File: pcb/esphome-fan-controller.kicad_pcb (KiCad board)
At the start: 2 copper layers, 25 x 42.5 mm, 50 parts, among them J1 Screw_Terminal_01x02, J2 USB-C, M1 Fan_CPU_4pin, SW1 BOOT, SW2 RESET, U1 MPM3506AGQV-P, U2 TPS61322DBZ, U3 ESP32-C3-MINI-1, U4 SN74LV1T34DBV, U5 SN74LV1T34DBV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

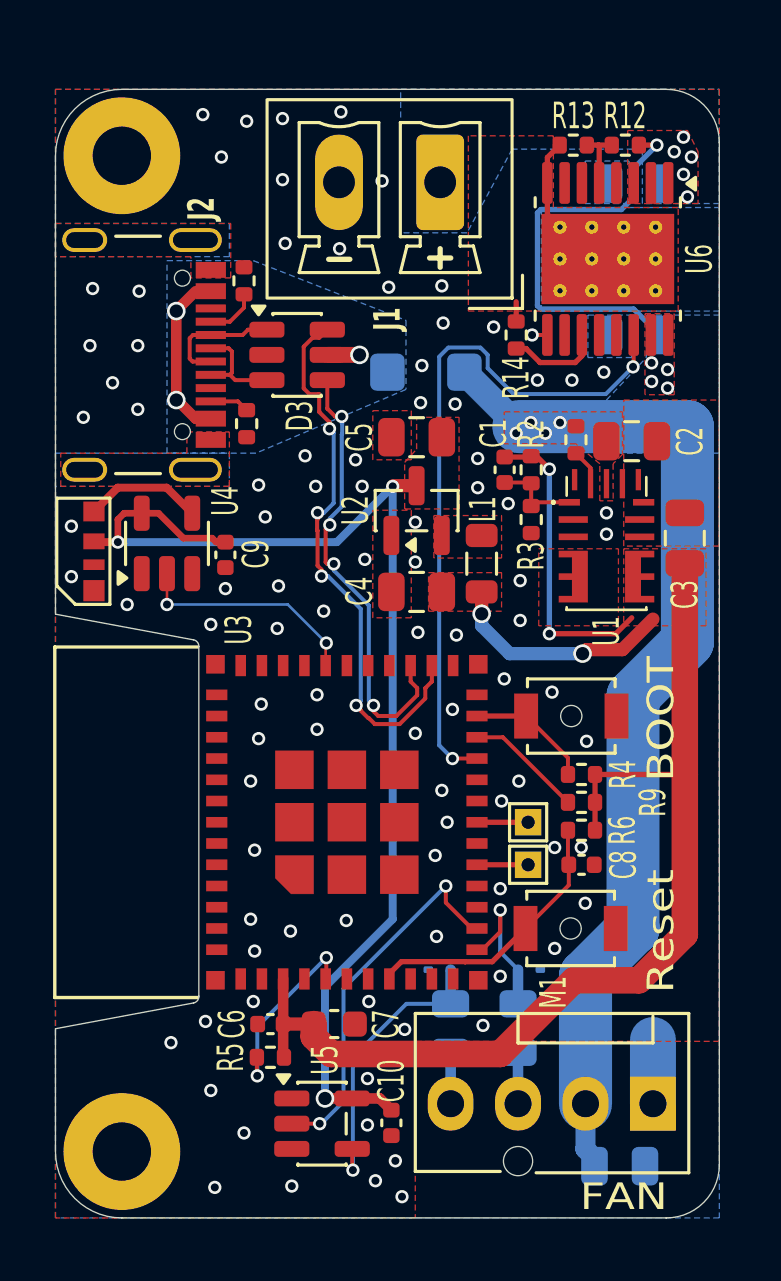
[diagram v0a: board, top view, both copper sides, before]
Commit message: Update PCB to Rev A 5V power supply now uses TPS613222A. Different package with correct voltage. Replace fan interface ESD diodes with dual TVS in SOT-23 package. Shutdown on LM76202 can be used to reduce fan power on 3-Pins. Add D4 to support 3-Pin fans. Move all components to top side.
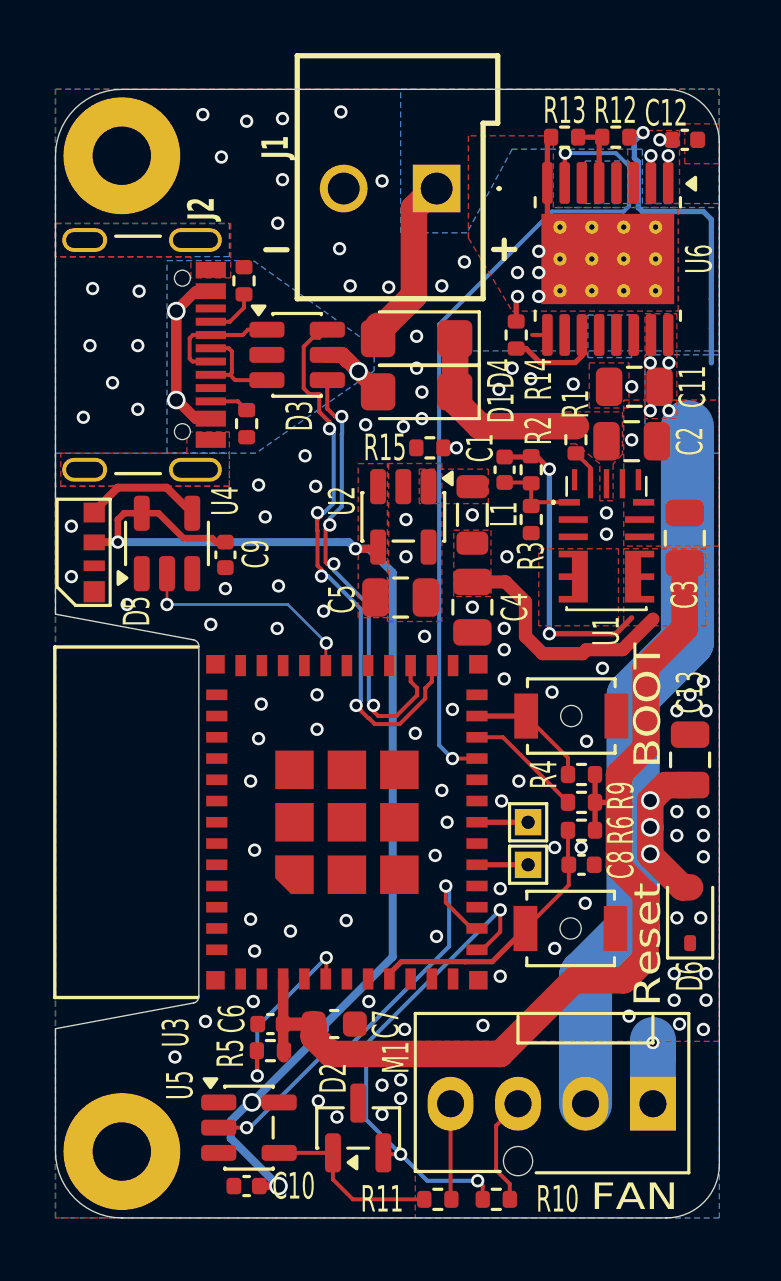
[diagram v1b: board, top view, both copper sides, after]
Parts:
- removed D7: ESD9B3.3ST5G, Diode_SMD:D_SOD-923
- added D2: ESDS452, Package_TO_SOT_SMD:SOT-23, F.Cu at (138.2, 61.8)
- added R15: 10KΩ, Resistor_SMD:R_0402_1005Metric, F.Cu at (140.8, 36.1)
- C11, C13, D1, D6: moved to F.Cu
- C12: value 1uF -> 100nF; footprint Capacitor_SMD:C_0805_2012Metric -> Capacitor_SMD:C_0402_1005Metric; moved to F.Cu
- D4: value ESD9B3.3ST5G -> SS2FH6HM3/H; footprint Diode_SMD:D_SOD-923 -> Diode_SMD:D_SMF; moved to F.Cu
- J1: footprint Connector_Phoenix_MC:PhoenixContact_MCV_1,5_2-G-3.81_1x02_P3.81mm_Vertical -> 1984769:1984769
- R10, R11: footprint Resistor_SMD:R_0805_2012Metric -> Resistor_SMD:R_0402_1005Metric; moved to F.Cu
- SW1: value BOOT -> ~
- SW2: value RESET -> ~
- U2: value TPS61322DBZ -> TPS613222ADBV; footprint Package_TO_SOT_SMD:SOT-23 -> Package_TO_SOT_SMD:SOT-23-5
- moved D4 24.1 mm to (140.3, 32.0)
- moved C13 15.5 mm to (150.7, 47.9), turned to -90 degrees
- moved D5 8.69 mm to (128.2, 40.2)
- moved R10 6.50 mm to (143.3, 64.5), turned to 0 degrees
- moved R11 6.47 mm to (141.2, 64.5), turned to 0 degrees
- moved C5 6.07 mm to (139.7, 41.8), turned to 0 degrees
- moved C10 5.95 mm to (133.9, 64.0), turned to 0 degrees
- moved D6 5.44 mm to (150.7, 53.8), turned to 90 degrees
- moved U5 2.75 mm to (134.0, 61.8)
- moved C12 2.52 mm to (150.4, 24.6), turned to 0 degrees
- moved C4 2.18 mm to (142.4, 42.1), turned to -90 degrees
- moved C11 1.95 mm to (148.6, 33.9)
- moved L1 1.87 mm to (142.4, 38.7)
- moved D1 0.82 mm to (140.3, 34.0)
- moved U2 0.55 mm to (139.8, 38.8), turned to -90 degrees
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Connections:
- C11 pad 1: VINT -> VFAN
- C13 pad 2: VINT -> VFAN
- D4 pad 1: GND -> VINT
- D4 pad 2: FAN_TACH -> VIN
- D6 pad 2: VINT -> VFAN
- M1 pad 2: VINT -> VFAN
- R12 pad 1: VINT -> VFAN
- U2 pad 1: GND -> /+5V_SW
- U2 pad 2: /+5V_SW -> GND
- U2 pad 3: +5V -> unconnected-(U2-NC-Pad3)
- U3 pad 21: FAULT -> ~{FAN_SHDN}
- U6 pad 14: FAULT -> unconnected-(U6-~{FLT}-Pad14)
- U6 pad 15: VINT -> VFAN
- U6 pad 16: VINT -> VFAN
- U6 pad 7: unconnected-(U6-~{SHDN}-Pad7) -> ~{FAN_SHDN}
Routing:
- net VINT: track 54.3 -> 7.30 mm, vias 9 -> 0
- net VFAN: track 0.00 -> 45.5 mm, vias 0 -> 8
- net ~{FAN_SHDN}: track 0.00 -> 32.9 mm, vias 0 -> 3
- net FAULT: track 26.4 -> 0.00 mm, vias 2 -> 0
- net FAN_TACH: track 5.79 -> 18.6 mm, vias 1 -> 3
- net VIN: track 0.00 -> 6.50 mm, vias 5 -> 3
- net Net-(U5-Y): track 10.9 -> 6.78 mm, vias 1 -> 0
- net Net-(M1-Tacho): track 1.94 -> 4.16 mm
- net FAN_PWM: track 14.2 -> 16.0 mm
- net Net-(M1-PWM): track 1.94 -> 3.61 mm
- net +3.3V: track 60.4 -> 58.9 mm, vias 4 -> 2
- net /VBUS: track 7.06 -> 8.51 mm
- net +5V: track 45.3 -> 46.2 mm, vias 3 -> 4
- net RTN: track 4.42 -> 4.58 mm, vias 0 -> 5
- net GND: vias 95 -> 113
- added copper zone on B.Cu, net VFAN
- added copper zone on F.Cu, net VFAN
- removed copper zone on B.Cu, net VINT
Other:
- board text added: "REV A 2026-03-14"
- board text removed: "REV - 2026-03-04"
